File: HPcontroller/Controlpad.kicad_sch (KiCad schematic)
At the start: 13 parts, among them J3 AudioJack4_Ground, J3 Conn_01x04_Pin, U5 MCP23017_SO

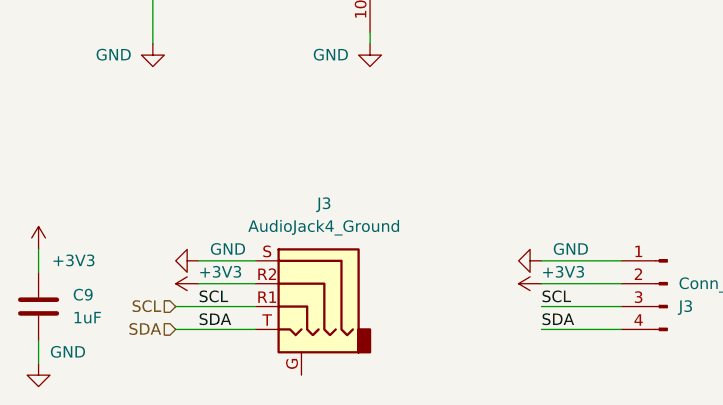
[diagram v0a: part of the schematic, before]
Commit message: started routing, finished footprintns
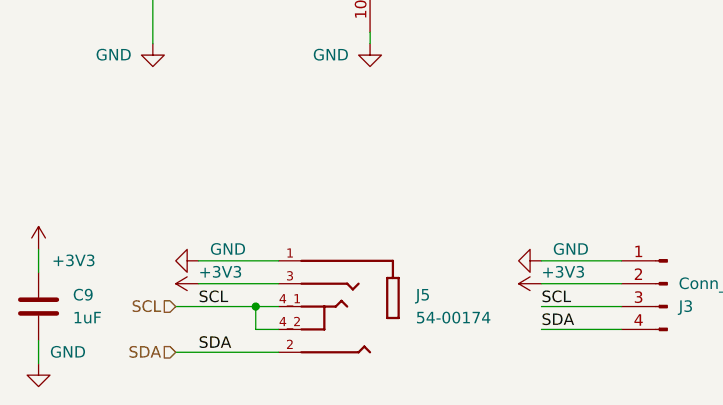
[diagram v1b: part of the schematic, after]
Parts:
- removed J3: AudioJack4_Ground, symbol Connector_Audio:AudioJack4_Ground
- added J5: 54-00174, TENSILITY_54-00174, symbol HPsym:54-00174
- J3: footprint (none) -> Connector_PinHeader_2.54mm:PinHeader_1x04_P2.54mm_Vertical
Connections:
- net +3V3: now also J5.3
- net GND: now also J5.1
- net SCL: now also J5.4_1, J5.4_2
- net SDA: now also J5.2
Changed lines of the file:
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@@
 (kicad_sch (version 20230121) (generator eeschema)
   (paper "A4")
+  (junction (at 83.82 132.08) (diameter 0) (color 0 0 0 0)
+  )
   (junction (at 72.39 91.44) (diameter 0) (color 0 0 0 0)
   )
@@
     (stroke (width 0) (type default))
   )
-  (wire (pts (xy 74.93 134.62) (xy 83.82 134.62))
+  (wire (pts (xy 74.93 137.16) (xy 86.36 137.16))
     (stroke (width 0) (type default))
   )
@@
     (stroke (width 0) (type default))
   )
+  (wire (pts (xy 83.82 132.08) (xy 86.36 132.08))
+    (stroke (width 0) (type default))
+  )
   (wire (pts (xy 203.2 96.52) (xy 234.95 96.52))
     (stroke (width 0) (type default))
@@
     (stroke (width 0) (type default))
   )
-  (wire (pts (xy 83.82 127) (xy 77.47 127))
-    (stroke (width 0) (type default))
-  )
-  (wire (pts (xy 77.47 129.54) (xy 83.82 129.54))
+  (wire (pts (xy 77.47 127) (xy 86.36 127))
+    (stroke (width 0) (type default))
+  )
+  (wire (pts (xy 77.47 129.54) (xy 86.36 129.54))
     (stroke (width 0) (type default))
   )
@@
     (stroke (width 0) (type default))
   )
+  (wire (pts (xy 83.82 134.62) (xy 83.82 132.08))
+    (stroke (width 0) (type default))
+  )
   (wire (pts (xy 72.39 88.9) (xy 72.39 91.44))
     (stroke (width 0) (type default))
   )
+  (wire (pts (xy 86.36 134.62) (xy 83.82 134.62))
+    (stroke (width 0) (type default))
+  )
   (wire (pts (xy 170.18 69.85) (xy 170.18 76.2))
     (stroke (width 0) (type default))
@@
     (effects (font (size 1.27 1.27)) (justify left bottom))
   )
-  (label "SDA" (at 77.47 134.62 0) (fields_autoplaced)
+  (label "SDA" (at 77.47 137.16 0) (fields_autoplaced)
     (effects (font (size 1.27 1.27)) (justify left bottom))
   )
@@
     (effects (font (size 1.27 1.27)) (justify right))
   )
-  (hierarchical_label "SDA" (shape input) (at 74.93 134.62 180) (fields_autoplaced)
+  (hierarchical_label "SDA" (shape input) (at 74.93 137.16 180) (fields_autoplaced)
     (effects (font (size 1.27 1.27)) (justify right))
   )
@@
     )
   )
+  (symbol (lib_id "HPsym:54-00174") (at 93.98 132.08 0) (mirror y) (unit 1)
+    (in_bom yes) (on_board yes) (dnp no) (fields_autoplaced)
+    (property "Reference" "J5" (at 101.6 130.81 0)
+      (effects (font (size 1.27 1.27)) (justify right))
+    )
+    (property "Value" "54-00174" (at 101.6 133.35 0)
+      (effects (font (size 1.27 1.27)) (justify right))
+    )
+    (property "Footprint" "TENSILITY_54-00174" (at 95.25 121.92 0)
+      (effects (font (size 1.27 1.27)) (justify left bottom) hide)
+    )
+    (property "Datasheet" "" (at 93.98 132.08 0)
+      (effects (font (size 1.27 1.27)) (justify left bottom) hide)
+    )
+    (property "PARTREV" "A" (at 80.01 128.27 0)
+      (effects (font (size 1.27 1.27)) (justify left bottom) hide)
+    )
+    (property "STANDARD" "Manufacturer Recommendations" (at 95.25 124.46 0)
+      (effects (font (size 1.27 1.27)) (justify left bottom) hide)
+    )
+    (property "SNAPEDA_PN" "54-00174" (at 74.93 121.92 0)
+      (effects (font (size 1.27 1.27)) (justify left bottom) hide)
+    )
+    (property "MAXIMUM_PACKAGE_HEIGHT" "6mm" (at 78.74 128.27 0)
+      (effects (font (size 1.27 1.27)) (justify left bottom) hide)
+    )
+    (property "MANUFACTURER" "TENSILITY" (at 77.47 130.81 0)
+      (effects (font (size 1.27 1.27)) (justify left bottom) hide)
+    )
+    (property "MPN" "54-00174" (at 93.98 132.08 0)
+      (effects (font (size 1.27 1.27)) hide)
+    )
+    (pin "1")
+    (pin "2")
+    (pin "3")
+    (pin "4_1")
+    (pin "4_2")
+    (instances
+      (project "HPcontroller"
+        (path "/e63e39d7-6ac0-4ffd-8aa3-1841a4541b55"
+          (reference "J5") (unit 1)
+        )
+        (path "/e63e39d7-6ac0-4ffd-8aa3-1841a4541b55/6f313458-fa7e-4b68-8821-33171d7f459a"
+          (reference "J1") (unit 1)
+        )
+      )
+    )
+  )
   (symbol (lib_id "power:GND") (at 82.55 44.45 0) (unit 1)
     (in_bom yes) (on_board yes) (dnp no)
@@
         )
         (path "/e63e39d7-6ac0-4ffd-8aa3-1841a4541b55/6f313458-fa7e-4b68-8821-33171d7f459a"
-          (reference "D_HEAT") (unit 1)
+          (reference "D_HEAT1") (unit 1)
         )
       )
@@
       (effects (font (size 1.27 1.27)) (justify right))
     )
-    (property "Footprint" "" (at 129.54 129.54 0)
+    (property "Footprint" "Connector_PinHeader_2.54mm:PinHeader_1x04_P2.54mm_Vertical" (at 129.54 129.54 0)
       (effects (font (size 1.27 1.27)) hide)
     )
@@
         )
         (path "/e63e39d7-6ac0-4ffd-8aa3-1841a4541b55/6f313458-fa7e-4b68-8821-33171d7f459a"
-          (reference "D_HOT") (unit 1)
+          (reference "D_HOT1") (unit 1)
         )
       )
@@
         )
         (path "/e63e39d7-6ac0-4ffd-8aa3-1841a4541b55/6f313458-fa7e-4b68-8821-33171d7f459a"
-          (reference "D_RUN") (unit 1)
+          (reference "D_RUN1") (unit 1)
         )
       )
@@
     )
   )
-  (symbol (lib_id "Connector_Audio:AudioJack4_Ground") (at 88.9 129.54 0) (mirror y) (unit 1)
-    (in_bom yes) (on_board yes) (dnp no)
-    (property "Reference" "J3" (at 91.44 120.65 0)
-      (effects (font (size 1.27 1.27)))
-    )
-    (property "Value" "AudioJack4_Ground" (at 91.44 123.19 0)
-      (effects (font (size 1.27 1.27)))
-    )
-    (property "Footprint" "" (at 88.9 129.54 0)
-      (effects (font (size 1.27 1.27)) hide)
-    )
-    (property "Datasheet" "~" (at 88.9 129.54 0)
-      (effects (font (size 1.27 1.27)) hide)
-    )
-    (pin "G")
-    (pin "R1")
-    (pin "R2")
-    (pin "S")
-    (pin "T")
-    (instances
-      (project "HPcontroller"
-        (path "/e63e39d7-6ac0-4ffd-8aa3-1841a4541b55"
-          (reference "J3") (unit 1)
-        )
-        (path "/e63e39d7-6ac0-4ffd-8aa3-1841a4541b55/6f313458-fa7e-4b68-8821-33171d7f459a"
-          (reference "J4") (unit 1)
-        )
-      )
-    )
-  )
   (symbol (lib_id "power:+3V3") (at 115.57 129.54 90) (unit 1)
     (in_bom yes) (on_board yes) (dnp no)
@@
         )
         (path "/e63e39d7-6ac0-4ffd-8aa3-1841a4541b55/6f313458-fa7e-4b68-8821-33171d7f459a"
-          (reference "D_POW") (unit 1)
-        )
-      )
+          (reference "D_POW1") (unit 1)
+        )
+      )

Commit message: finished routing, moving on to heater
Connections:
- net DEC: now also U5.22 (GPA1); no longer U5.23 (GPA2)
- net INC: now also U5.23 (GPA2); no longer U5.22 (GPA1)
- net RUN: no longer D_RUN1.2 (A), U5.2 (GPB1)
- new net RUN_LED: D_RUN1.2 (A), U5.2 (GPB1)
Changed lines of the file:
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@@
     (stroke (width 0) (type default))
   )
-  (label "INC" (at 116.84 78.74 0) (fields_autoplaced)
+  (label "INC" (at 116.84 81.28 0) (fields_autoplaced)
     (effects (font (size 1.27 1.27)) (justify left bottom))
   )
@@
     (effects (font (size 1.27 1.27)) (justify left bottom))
   )
-  (label "DEC" (at 116.84 81.28 0) (fields_autoplaced)
+  (label "DEC" (at 116.84 78.74 0) (fields_autoplaced)
     (effects (font (size 1.27 1.27)) (justify left bottom))
   )
@@
     (effects (font (size 1.27 1.27)) (justify left bottom))
   )
-  (label "RUN" (at 116.84 55.88 0) (fields_autoplaced)
+  (label "RUN_LED" (at 116.84 55.88 0) (fields_autoplaced)
     (effects (font (size 1.27 1.27)) (justify left bottom))
   )
@@
     (effects (font (size 1.27 1.27)) (justify left bottom))
   )
-  (label "RUN" (at 203.2 96.52 0) (fields_autoplaced)
+  (label "RUN_LED" (at 203.2 96.52 0) (fields_autoplaced)
     (effects (font (size 1.27 1.27)) (justify left bottom))
   )

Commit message: worked on bom, orderables from dk are in
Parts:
- C5, C9: Digikey PN (none) -> 1276-1066-1-ND; MPN (none) -> CL21B105KAFNNNE
- J5: Digikey PN (none) -> 839-54-00174CT-ND; SNAPEDA_PN 54-00174 -> (none)
- SWDEC1, SWINC1, SWINC2, SWRUN1: Digikey PN (none) -> CKN9112CT-ND; MPN (none) -> PTS645SM43SMTR92 LFS
- U5: Digikey PN (none) -> MCP23017T-E/SOCT-ND; MPN (none) -> MCP23017T-E/SO
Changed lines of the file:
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@@
+      (effects (font (size 1.27 1.27)) hide)
+    )
+    (property "Digikey PN" "1276-1066-1-ND" (at 59.69 132.08 0)
+      (effects (font (size 1.27 1.27)) hide)
+    )
+    (property "MPN" "CL21B105KAFNNNE" (at 59.69 132.08 0)
       (effects (font (size 1.27 1.27)) hide)
     )
@@
       (effects (font (size 1.27 1.27)) (justify left bottom) hide)
     )
-    (property "SNAPEDA_PN" "54-00174" (at 74.93 121.92 0)
+    (property "SNAPEDA_PN" "" (at 74.93 121.92 0)
       (effects (font (size 1.27 1.27)) (justify left bottom) hide)
     )
@@
     )
     (property "MPN" "54-00174" (at 93.98 132.08 0)
+      (effects (font (size 1.27 1.27)) hide)
+    )
+    (property "Digikey PN" "839-54-00174CT-ND" (at 93.98 132.08 0)
       (effects (font (size 1.27 1.27)) hide)
     )
@@
       (effects (font (size 1.27 1.27)) hide)
     )
+    (property "Digikey PN" "CKN9112CT-ND" (at 161.29 69.85 0)
+      (effects (font (size 1.27 1.27)) hide)
+    )
+    (property "MPN" "PTS645SM43SMTR92 LFS" (at 161.29 69.85 0)
+      (effects (font (size 1.27 1.27)) hide)
+    )
     (pin "1")
     (pin "2")
@@
     )
     (property "Datasheet" "~" (at 82.55 39.37 0)
+      (effects (font (size 1.27 1.27)) hide)
+    )
+    (property "Digikey PN" "1276-1066-1-ND" (at 82.55 39.37 0)
+      (effects (font (size 1.27 1.27)) hide)
+    )
+    (property "MPN" "CL21B105KAFNNNE" (at 82.55 39.37 0)
       (effects (font (size 1.27 1.27)) hide)
     )
@@
       (effects (font (size 1.27 1.27)) hide)
     )
+    (property "Digikey PN" "CKN9112CT-ND" (at 161.29 60.96 0)
+      (effects (font (size 1.27 1.27)) hide)
+    )
+    (property "MPN" "PTS645SM43SMTR92 LFS" (at 161.29 60.96 0)
+      (effects (font (size 1.27 1.27)) hide)
+    )
     (pin "1")
     (pin "2")
@@
       (effects (font (size 1.27 1.27)) hide)
     )
+    (property "Digikey PN" "CKN9112CT-ND" (at 161.29 43.18 0)
+      (effects (font (size 1.27 1.27)) hide)
+    )
+    (property "MPN" "PTS645SM43SMTR92 LFS" (at 161.29 43.18 0)
+      (effects (font (size 1.27 1.27)) hide)
+    )
     (pin "1")
     (pin "2")
@@
     )
     (property "Datasheet" "~" (at 161.29 52.07 0)
+      (effects (font (size 1.27 1.27)) hide)
+    )
+    (property "Digikey PN" "CKN9112CT-ND" (at 161.29 52.07 0)
+      (effects (font (size 1.27 1.27)) hide)
+    )
+    (property "MPN" "PTS645SM43SMTR92 LFS" (at 161.29 52.07 0)
       (effects (font (size 1.27 1.27)) hide)
     )
@@
       (effects (font (size 1.27 1.27)) (justify left) hide)
     )
-    (pin "1")
+    (property "Digikey PN" "MCP23017T-E/SOCT-ND" (at 96.52 73.66 0)
+      (effects (font (size 1.27 1.27)) hide)
+    )
+    (property "MPN" "MCP23017T-E/SO" (at 96.52 73.66 0)
+      (effects (font (size 1.27 1.27)) hide)
+    )
+    (pin "1")

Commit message: v3 routing
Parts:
- renumbered D_RUN1 to D_HEAT1, D_3V3_POW1 to D_POW1, J5 to J1, SWDEC1 to SWDEC2, SWINC2 to SWINC3, SWINC1 to SWINC4, SWRUN1 to SWRUN2, U5 to U1
